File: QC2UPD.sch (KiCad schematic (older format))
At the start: 16 parts

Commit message: Add USB-PD comment
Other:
- note added: "10k pullup on CC pin -> USB PD 3A current"
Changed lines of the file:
@@
 Wire Wire Line
 	1700 1400 1700 1000
+Text Notes 8000 4400 0    60   ~ 0
+10k pullup on CC pin -> USB PD 3A current
 $EndSCHEMATC

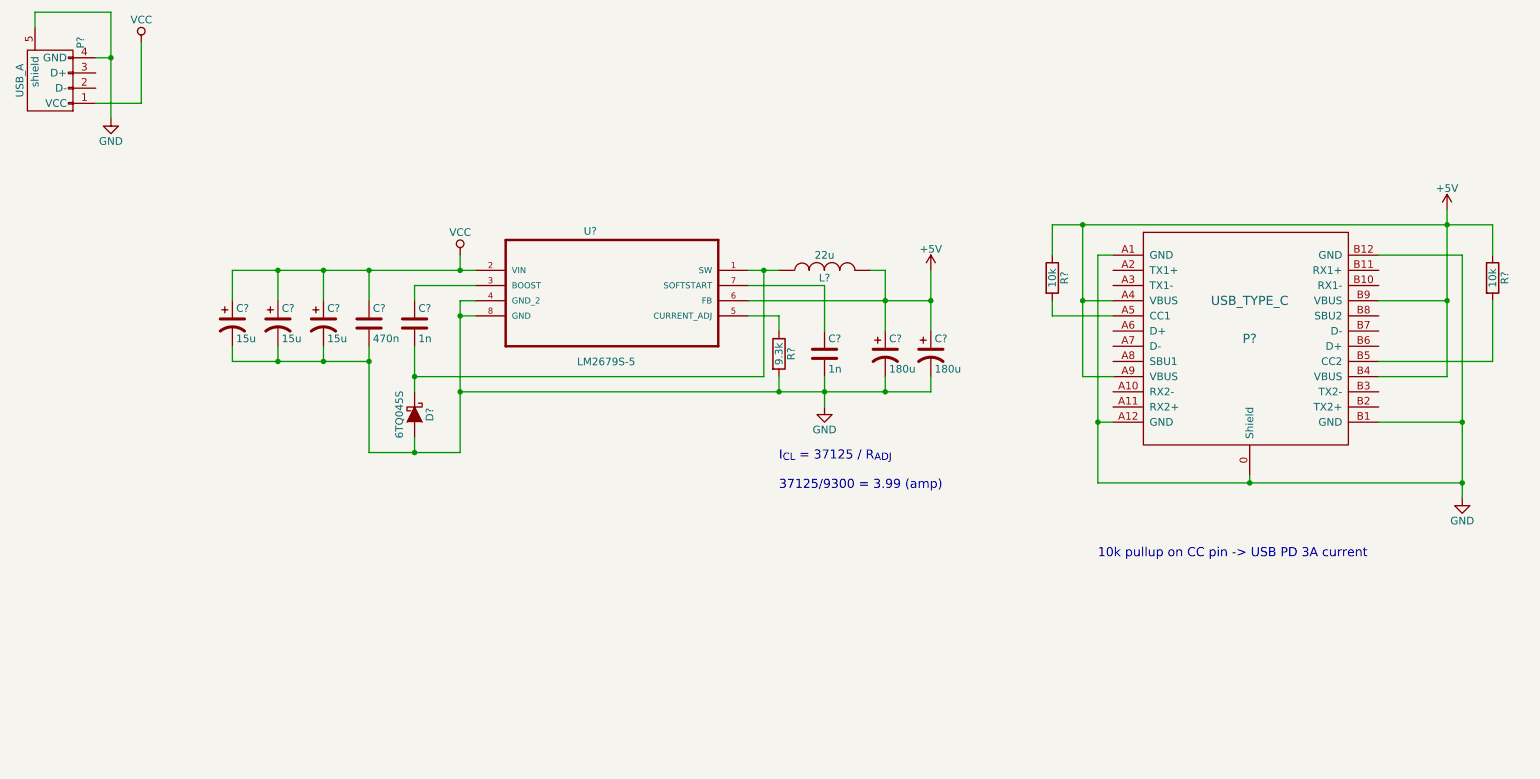
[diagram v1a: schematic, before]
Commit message: QC 2.0 voltage ref
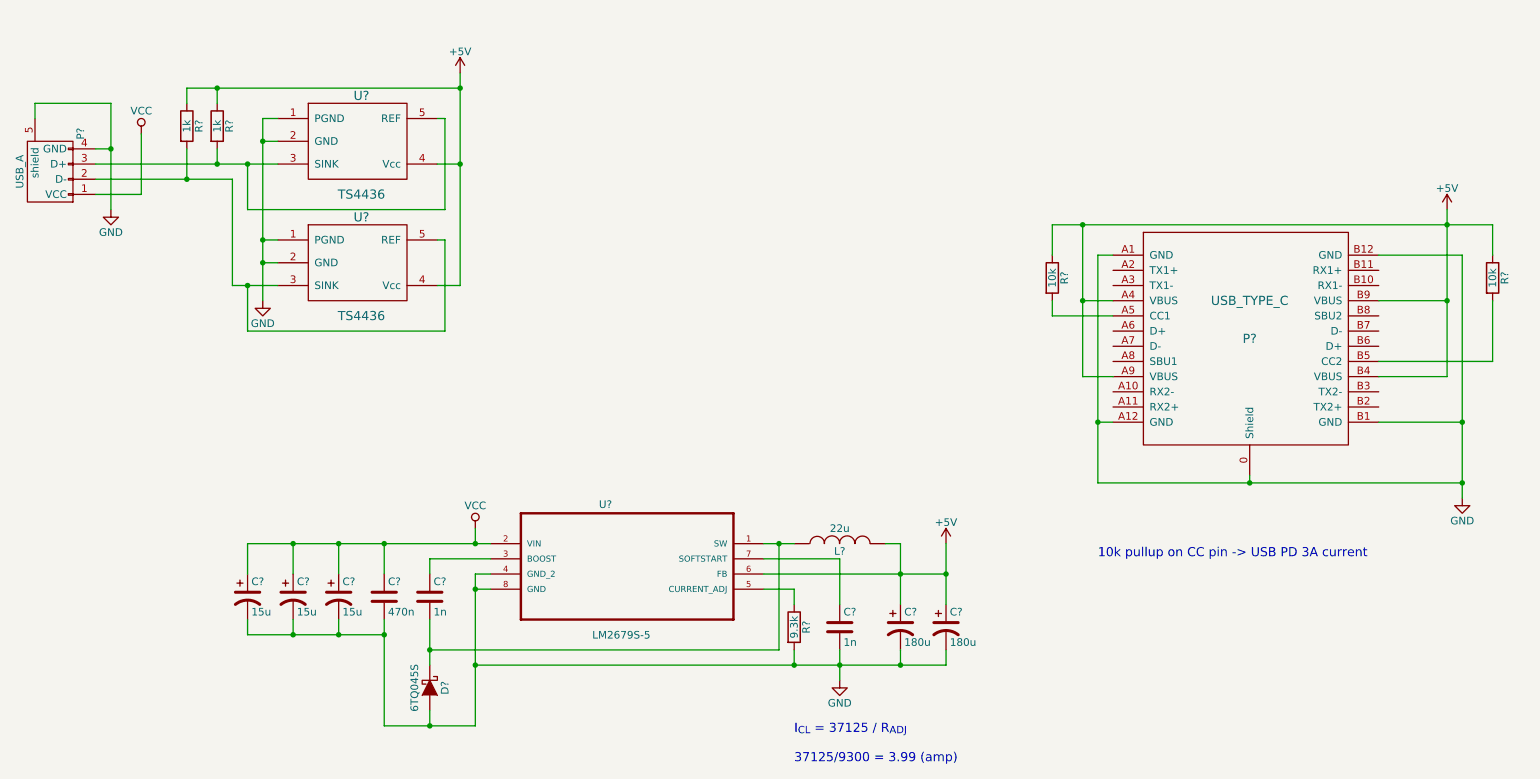
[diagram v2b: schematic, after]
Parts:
- added R? (x2): 1k, symbol R
- added U? (x2): TS4436, symbol TS4436
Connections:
- net +5V: now also R?.1, R?.1, U?.4 (Vcc), U?.4 (Vcc)
- net GND: now also U?.1 (PGND), U?.1 (PGND), U?.2 (GND), U?.2 (GND)
- net at P?.2 (D-): now also R?.2, U?.3 (SINK), U?.5 (REF)
- net at P?.3 (D+): now also R?.2, U?.3 (SINK), U?.5 (REF)
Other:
- moved on the sheet: C?, D?, L?, P?, R?, U?

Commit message: Circuit cleanup, Remove unnecessary components
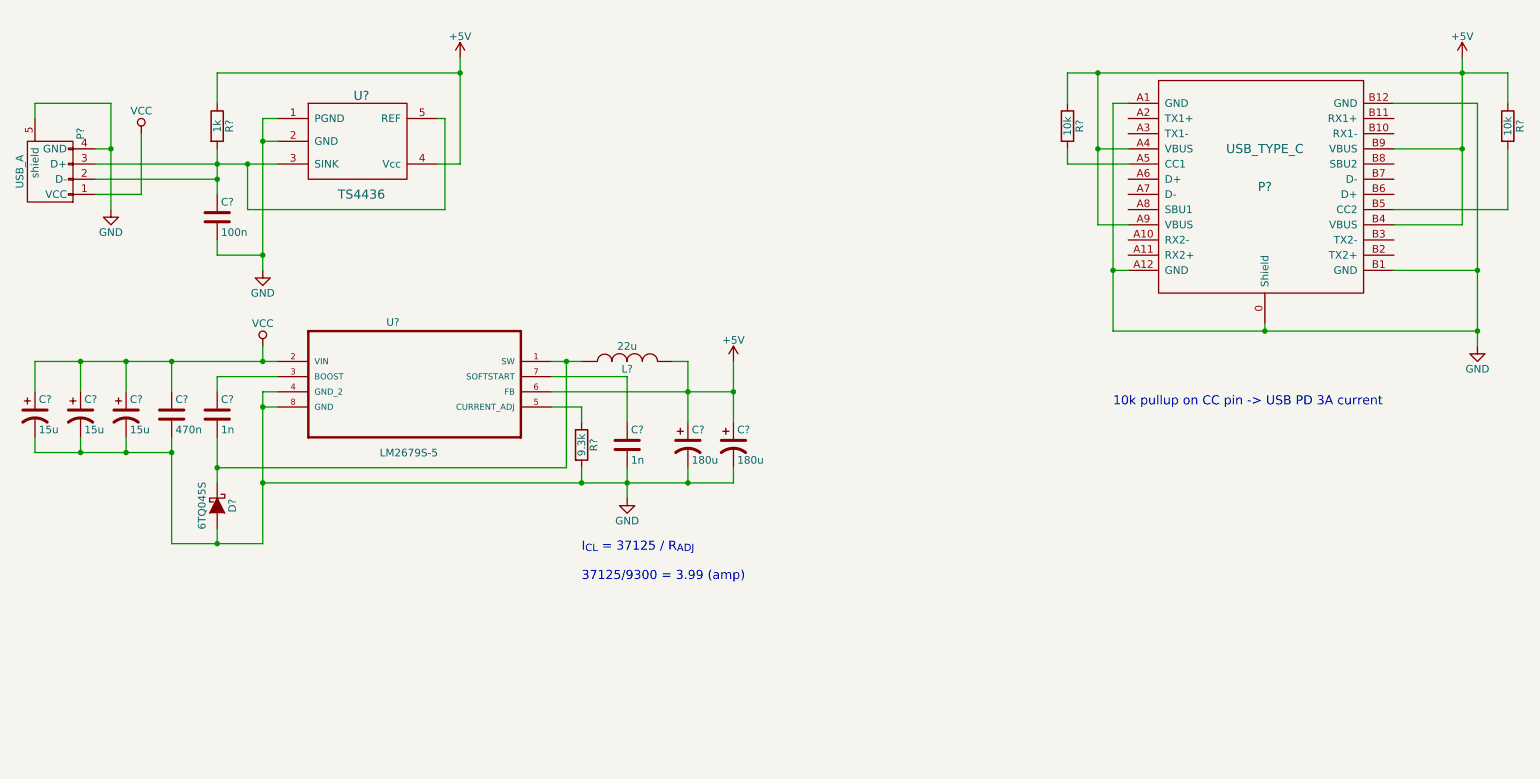
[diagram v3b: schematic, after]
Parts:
- removed R?: 1k, symbol R
- removed U?: TS4436, symbol TS4436
- added C?: 100n, symbol C
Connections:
- net GND: now also C?.2
- net at P?.2 (D-): now also P?.3 (D+), R?.2, U?.3 (SINK), U?.5 (REF), C?.1
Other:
- moved on the sheet: C?, D?, L?, P?, R?, U?

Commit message: Annotate parts
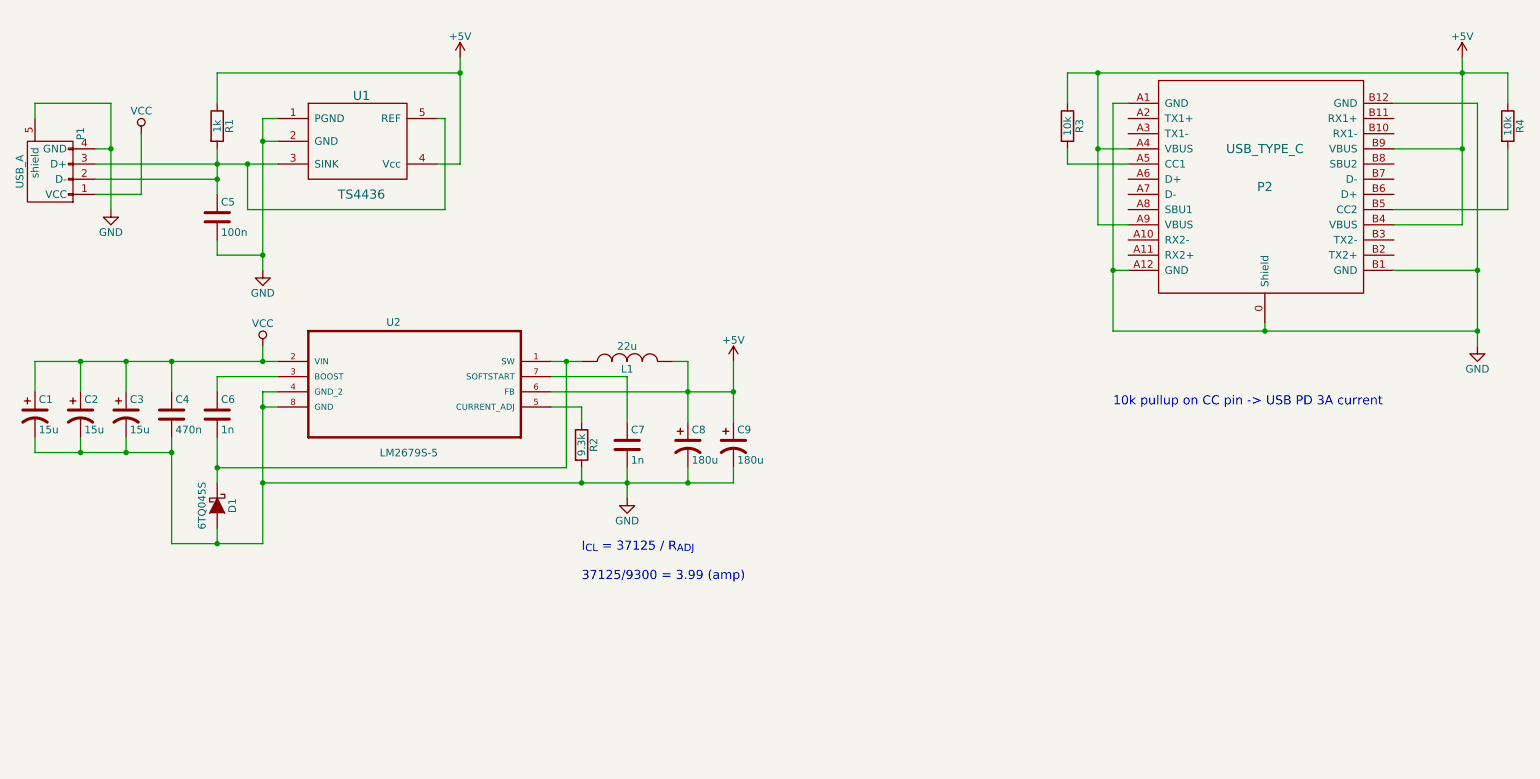
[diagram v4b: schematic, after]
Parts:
- gave numbers to parts that had none: 19
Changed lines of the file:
@@
 $EndDescr
 $Comp
-L USB_A P?
+L USB_A P1
 U 1 1 57B47A32
 P 1100 1800
-F 0 "P?" H 1300 1600 50  0000 C CNN
+F 0 "P1" H 1300 1600 50  0000 C CNN
 F 1 "USB_A" H 1050 2000 50  0000 C CNN
 F 2 "" V 1050 1700 50  0000 C CNN
@@
 $EndComp
 $Comp
-L USB_TYPE_C P?
+L USB_TYPE_C P2
 U 1 1 57B48023
 P 9100 1950
-F 0 "P?" H 9100 1950 60  0000 C CNN
+F 0 "P2" H 9100 1950 60  0000 C CNN
 F 1 "USB_TYPE_C" H 9100 2200 60  0000 C CNN
 F 2 "" H 9100 1950 60  0000 C CNN
@@
 $EndComp
 $Comp
-L GND #PWR?
+L GND #PWR9
 U 1 1 57B480B2
 P 10500 3000
-F 0 "#PWR?" H 10500 2750 50  0001 C CNN
+F 0 "#PWR9" H 10500 2750 50  0001 C CNN
 F 1 "GND" H 10500 2850 50  0000 C CNN
 F 2 "" H 10500 3000 50  0000 C CNN
@@
 $EndComp
 $Comp
-L +5V #PWR?
+L +5V #PWR8
 U 1 1 57B480FF
 P 10400 1100
-F 0 "#PWR?" H 10400 950 50  0001 C CNN
+F 0 "#PWR8" H 10400 950 50  0001 C CNN
 F 1 "+5V" H 10400 1240 50  0000 C CNN
 F 2 "" H 10400 1100 50  0000 C CNN
@@
 $EndComp
 $Comp
-L R R?
+L R R3
 U 1 1 57B48169
 P 7800 1550
-F 0 "R?" V 7880 1550 50  0000 C CNN
+F 0 "R3" V 7880 1550 50  0000 C CNN
 F 1 "10k" V 7800 1550 50  0000 C CNN
 F 2 "" V 7730 1550 50  0000 C CNN
@@
 $EndComp
 $Comp
-L R R?
+L R R4
 U 1 1 57B481CC
 P 10700 1550
-F 0 "R?" V 10780 1550 50  0000 C CNN
+F 0 "R4" V 10780 1550 50  0000 C CNN
 F 1 "10k" V 10700 1550 50  0000 C CNN
 F 2 "" V 10630 1550 50  0000 C CNN
@@
 $EndComp
 $Comp
-L LM2679S-5 U?
+L LM2679S-5 U2
 U 1 1 57B485EF
 P 3500 3100
-F 0 "U?" H 3314 3358 50  0000 L CNN
+F 0 "U2" H 3314 3358 50  0000 L CNN
 F 1 "LM2679S-5" H 3270 2498 50  0000 L CNN
 F 2 "TO127P1435X457-8N" H 3500 3100 50  0001 L CNN
@@
 $EndComp
 $Comp
-L CP1 C?
+L CP1 C2
 U 1 1 57B48AB2
 P 1300 3450
-F 0 "C?" H 1325 3550 50  0000 L CNN
+F 0 "C2" H 1325 3550 50  0000 L CNN
 F 1 "15u" H 1325 3350 50  0000 L CNN
 F 2 "" H 1300 3450 50  0000 C CNN
@@
 $EndComp
 $Comp
-L CP1 C?
+L CP1 C3
 U 1 1 57B48B0C
 P 1600 3450
-F 0 "C?" H 1625 3550 50  0000 L CNN
+F 0 "C3" H 1625 3550 50  0000 L CNN
 F 1 "15u" H 1625 3350 50  0000 L CNN
 F 2 "" H 1600 3450 50  0000 C CNN
@@
 $EndComp
 $Comp
-L CP1 C?
+L CP1 C1
 U 1 1 57B48B33
 P 1000 3450
-F 0 "C?" H 1025 3550 50  0000 L CNN
+F 0 "C1" H 1025 3550 50  0000 L CNN
 F 1 "15u" H 1025 3350 50  0000 L CNN
 F 2 "" H 1000 3450 50  0000 C CNN
@@
 $EndComp
 $Comp
-L C C?
+L C C4
 U 1 1 57B48FB5
 P 1900 3450
-F 0 "C?" H 1925 3550 50  0000 L CNN
+F 0 "C4" H 1925 3550 50  0000 L CNN
 F 1 "470n" H 1925 3350 50  0000 L CNN
 F 2 "" H 1938 3300 50  0000 C CNN
@@
 $EndComp
 $Comp
-L C C?
+L C C7
 U 1 1 57B490C5
 P 4900 3650
-F 0 "C?" H 4925 3750 50  0000 L CNN
+F 0 "C7" H 4925 3750 50  0000 L CNN
 F 1 "1n" H 4925 3550 50  0000 L CNN
 F 2 "" H 4938 3500 50  0000 C CNN
@@
 $EndComp
 $Comp
-L R R?
+L R R2
 U 1 1 57B49394
 P 4600 3650
-F 0 "R?" V 4680 3650 50  0000 C CNN
+F 0 "R2" V 4680 3650 50  0000 C CNN
 F 1 "9.3k" V 4600 3650 50  0000 C CNN
 F 2 "" V 4530 3650 50  0000 C CNN
@@
 $EndComp
 $Comp
-L C C?
+L C C6
 U 1 1 57B496B5
 P 2200 3450
-F 0 "C?" H 2225 3550 50  0000 L CNN
+F 0 "C6" H 2225 3550 50  0000 L CNN
 F 1 "1n" H 2225 3350 50  0000 L CNN
 F 2 "" H 2238 3300 50  0000 C CNN
@@
 $EndComp
 $Comp
-L VCC #PWR?
+L VCC #PWR4
 U 1 1 57B49778
 P 2500 3000
-F 0 "#PWR?" H 2500 2850 50  0001 C CNN
+F 0 "#PWR4" H 2500 2850 50  0001 C CNN
 F 1 "VCC" H 2500 3150 50  0000 C CNN
 F 2 "" H 2500 3000 50  0000 C CNN
@@
 $EndComp
 $Comp
-L GND #PWR?
+L GND #PWR6
 U 1 1 57B49E14
 P 4900 4000
-F 0 "#PWR?" H 4900 3750 50  0001 C CNN
+F 0 "#PWR6" H 4900 3750 50  0001 C CNN
 F 1 "GND" H 4900 3850 50  0000 C CNN
 F 2 "" H 4900 4000 50  0000 C CNN
@@
 $EndComp
 $Comp
-L D_Schottky D?
+L D_Schottky D1
 U 1 1 57B4A00F
 P 2200 4050
-F 0 "D?" H 2200 4150 50  0000 C CNN
+F 0 "D1" H 2200 4150 50  0000 C CNN
 F 1 "6TQ045S" H 2200 3950 50  0000 C CNN
 F 2 "" H 2200 4050 50  0000 C CNN
@@
 $EndComp
 $Comp
-L INDUCTOR L?
+L INDUCTOR L1
 U 1 1 57B4A1C6
 P 4900 3100
-F 0 "L?" V 4850 3100 50  0000 C CNN
+F 0 "L1" V 4850 3100 50  0000 C CNN
 F 1 "22u" V 5000 3100 50  0000 C CNN
 F 2 "" H 4900 3100 50  0000 C CNN
@@
 $EndComp
 $Comp
-L CP1 C?
+L CP1 C8
 U 1 1 57B4A32D
 P 5300 3650
-F 0 "C?" H 5325 3750 50  0000 L CNN
+F 0 "C8" H 5325 3750 50  0000 L CNN
 F 1 "180u" H 5325 3550 50  0000 L CNN
 F 2 "" H 5300 3650 50  0000 C CNN
@@
 $EndComp
 $Comp
-L CP1 C?
+L CP1 C9
 U 1 1 57B4A394
 P 5600 3650
-F 0 "C?" H 5625 3750 50  0000 L CNN
+F 0 "C9" H 5625 3750 50  0000 L CNN
 F 1 "180u" H 5625 3550 50  0000 L CNN
 F 2 "" H 5600 3650 50  0000 C CNN
@@
 $EndComp
 $Comp
-L +5V #PWR?
+L +5V #PWR7
 U 1 1 57B4A5EE
 P 5600 3100
-F 0 "#PWR?" H 5600 2950 50  0001 C CNN
+F 0 "#PWR7" H 5600 2950 50  0001 C CNN
 F 1 "+5V" H 5600 3240 50  0000 C CNN
 F 2 "" H 5600 3100 50  0000 C CNN
@@
 I_{CL} = 37125 / R_{ADJ}\n\n37125/9300 = 3.99 (amp)
 $Comp
-L GND #PWR?
+L GND #PWR1
 U 1 1 57B4B6E4
 P 1500 2100
-F 0 "#PWR?" H 1500 1850 50  0001 C CNN
+F 0 "#PWR1" H 1500 1850 50  0001 C CNN
 F 1 "GND" H 1500 1950 50  0000 C CNN
 F 2 "" H 1500 2100 50  0000 C CNN
@@
 $EndComp
 $Comp
-L VCC #PWR?
+L VCC #PWR2
 U 1 1 57B4B780
 P 1700 1600
-F 0 "#PWR?" H 1700 1450 50  0001 C CNN
+F 0 "#PWR2" H 1700 1450 50  0001 C CNN
 F 1 "VCC" H 1700 1750 50  0000 C CNN
 F 2 "" H 1700 1600 50  0000 C CNN
@@
 10k pullup on CC pin -> USB PD 3A current
 $Comp
-L TS4436 U?
+L TS4436 U1
 U 1 1 57B554A5
 P 3150 1650
-F 0 "U?" H 3150 1950 60  0000 C CNN
+F 0 "U1" H 3150 1950 60  0000 C CNN
 F 1 "TS4436" H 3150 1300 60  0000 C CNN
 F 2 "" H 3150 1650 60  0001 C CNN
@@
 $EndComp
 $Comp
-L GND #PWR?
+L GND #PWR3
 U 1 1 57B55ABB
 P 2500 2500
-F 0 "#PWR?" H 2500 2250 50  0001 C CNN
+F 0 "#PWR3" H 2500 2250 50  0001 C CNN
 F 1 "GND" H 2500 2350 50  0000 C CNN
 F 2 "" H 2500 2500 50  0000 C CNN
@@
 $EndComp
 $Comp
-L +5V #PWR?
+L +5V #PWR5
 U 1 1 57B55CC2
 P 3800 1100
-F 0 "#PWR?" H 3800 950 50  0001 C CNN
+F 0 "#PWR5" H 3800 950 50  0001 C CNN
 F 1 "+5V" H 3800 1240 50  0000 C CNN
 F 2 "" H 3800 1100 50  0000 C CNN
@@
 $EndComp
 $Comp
-L R R?
+L R R1
 U 1 1 57B565B4
 P 2200 1550
-F 0 "R?" V 2280 1550 50  0000 C CNN
+F 0 "R1" V 2280 1550 50  0000 C CNN
 F 1 "1k" V 2200 1550 50  0000 C CNN
 F 2 "" V 2130 1550 50  0000 C CNN
@@
 Connection ~ 3800 1200
 $Comp
-L C C?
+L C C5
 U 1 1 57B573B8
 P 2200 2150
-F 0 "C?" H 2225 2250 50  0000 L CNN
+F 0 "C5" H 2225 2250 50  0000 L CNN
 F 1 "100n" H 2225 2050 50  0000 L CNN
 F 2 "" H 2238 2000 50  0000 C CNN
